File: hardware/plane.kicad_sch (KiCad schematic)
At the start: 44 parts, among them J1 USB_B_Micro, J2 Conn_Coaxial, J3 Conn_01x03, J4 Conn_01x03, J5 Conn_01x03, J6 Conn_01x03, Q1 BSS138, Q2 BSS138, U1 ESP32-WROOM-32, U2 AMS1117-3.3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

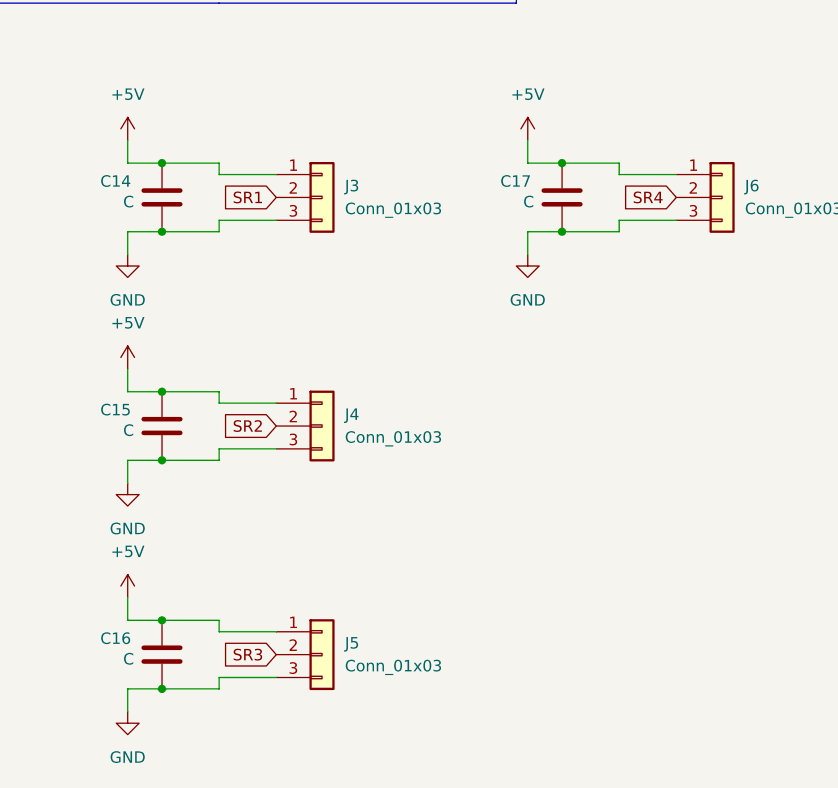
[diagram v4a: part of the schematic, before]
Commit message: add servo pin + wiring pcb
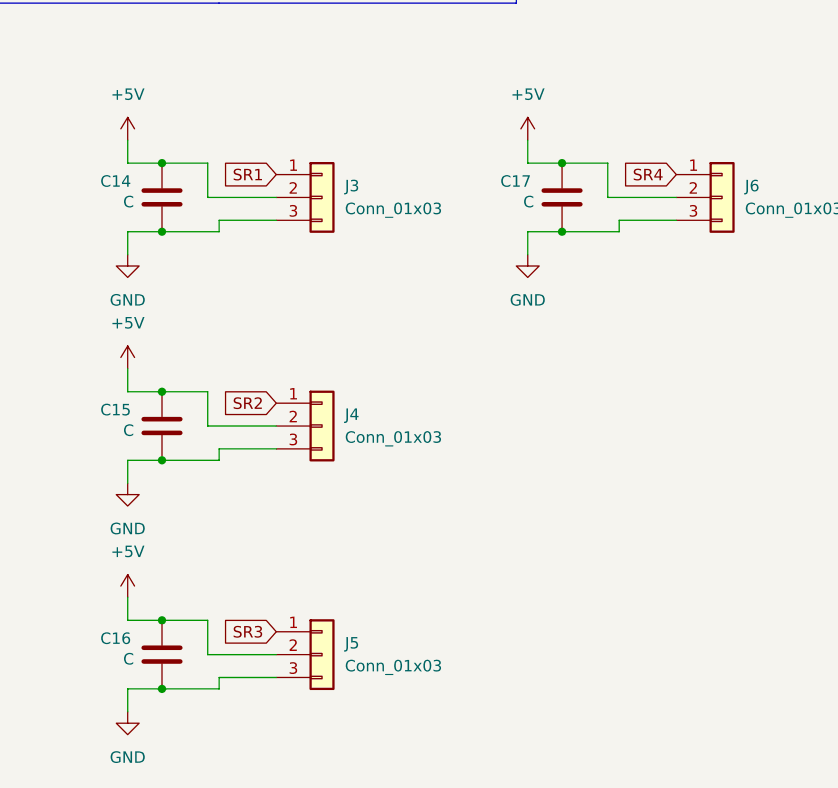
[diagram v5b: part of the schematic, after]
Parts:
- J3, J4, J5, J6: footprint (none) -> Connector_PinHeader_2.54mm:PinHeader_1x03_P2.54mm_Vertical
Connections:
- net +5V: now also J3.2 (Pin_2), J4.2 (Pin_2), J5.2 (Pin_2), J6.2 (Pin_2); no longer J3.1 (Pin_1), J4.1 (Pin_1), J5.1 (Pin_1), J6.1 (Pin_1)
- net SR1: now also J3.1 (Pin_1); no longer J3.2 (Pin_2)
- net SR2: now also J4.1 (Pin_1); no longer J4.2 (Pin_2)
- net SR3: now also J5.1 (Pin_1); no longer J5.2 (Pin_2)
- net SR4: now also J6.1 (Pin_1); no longer J6.2 (Pin_2)

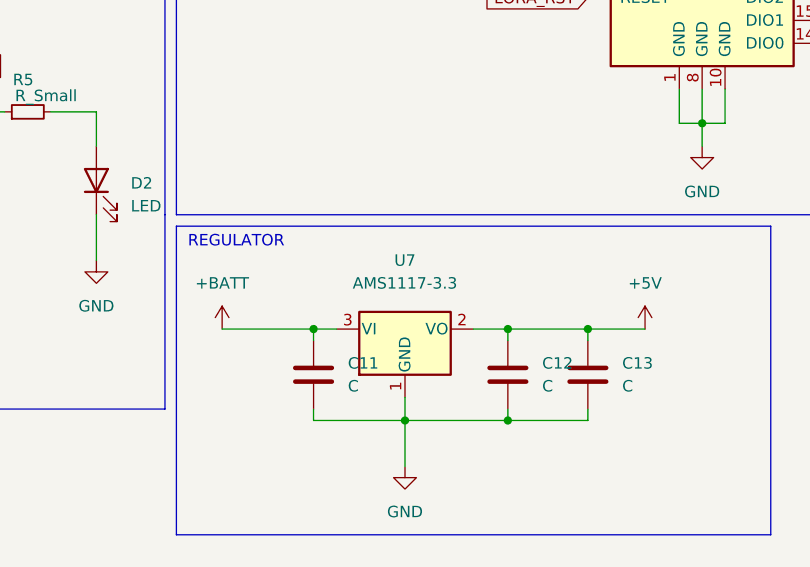
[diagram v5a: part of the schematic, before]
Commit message: wiring servo
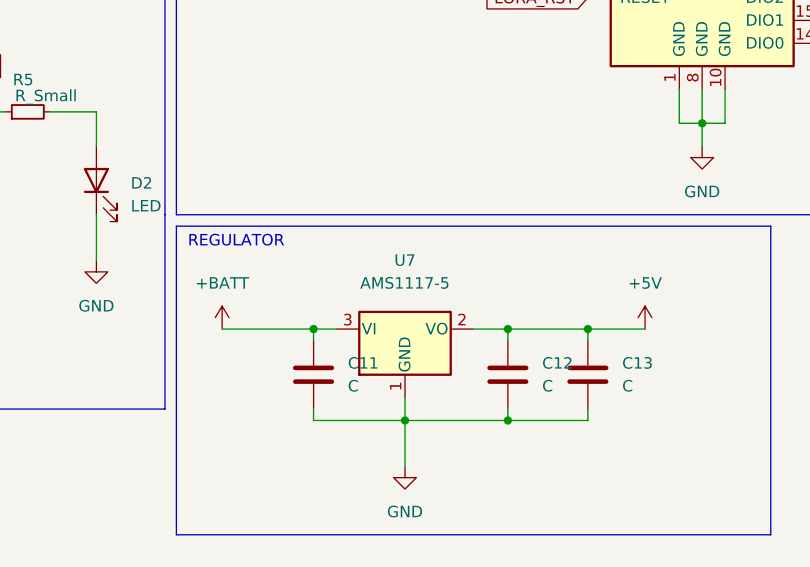
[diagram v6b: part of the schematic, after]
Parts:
- U7: value AMS1117-3.3 -> AMS1117-5
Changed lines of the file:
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@@
 			)
 		)
-		(property "Value" "AMS1117-3.3"
+		(property "Value" "AMS1117-5"
 			(at 137.16 129.54 0)
 			(effects

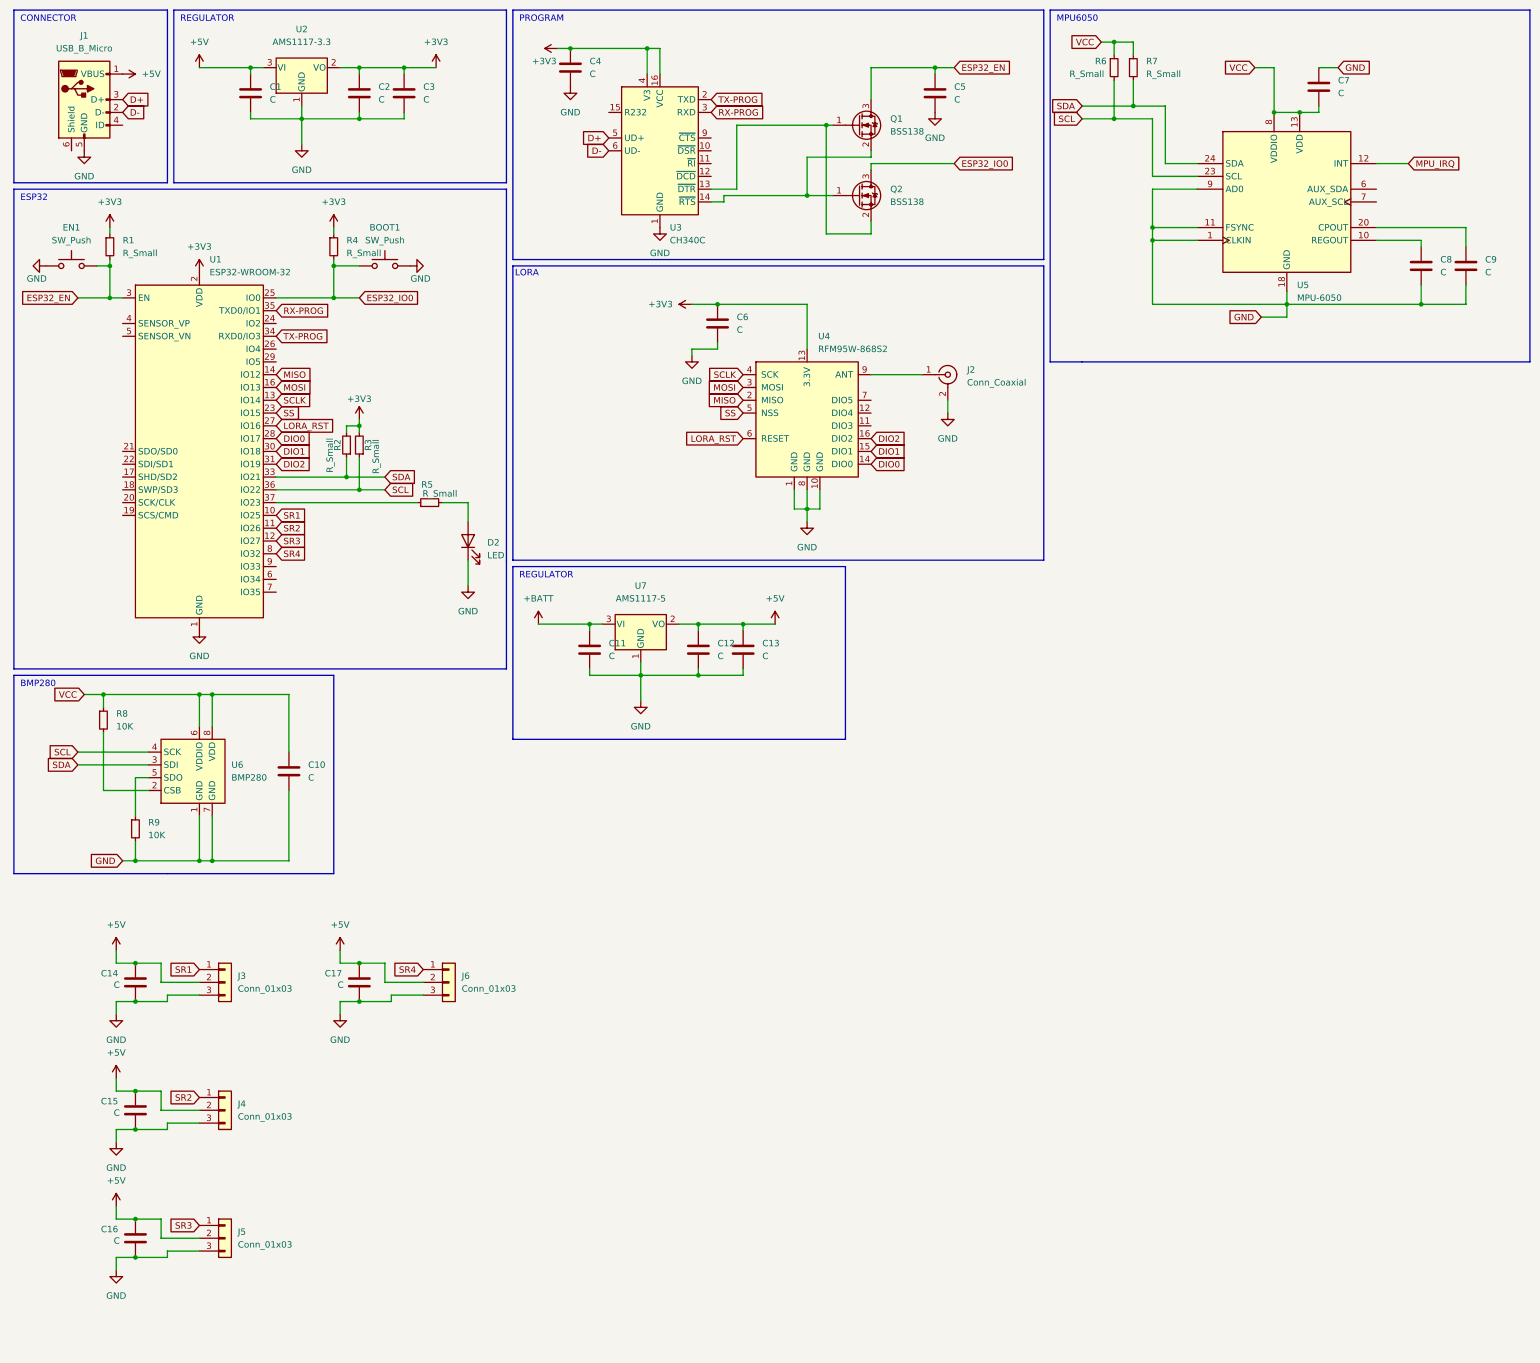
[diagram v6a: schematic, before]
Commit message: i2c wiring
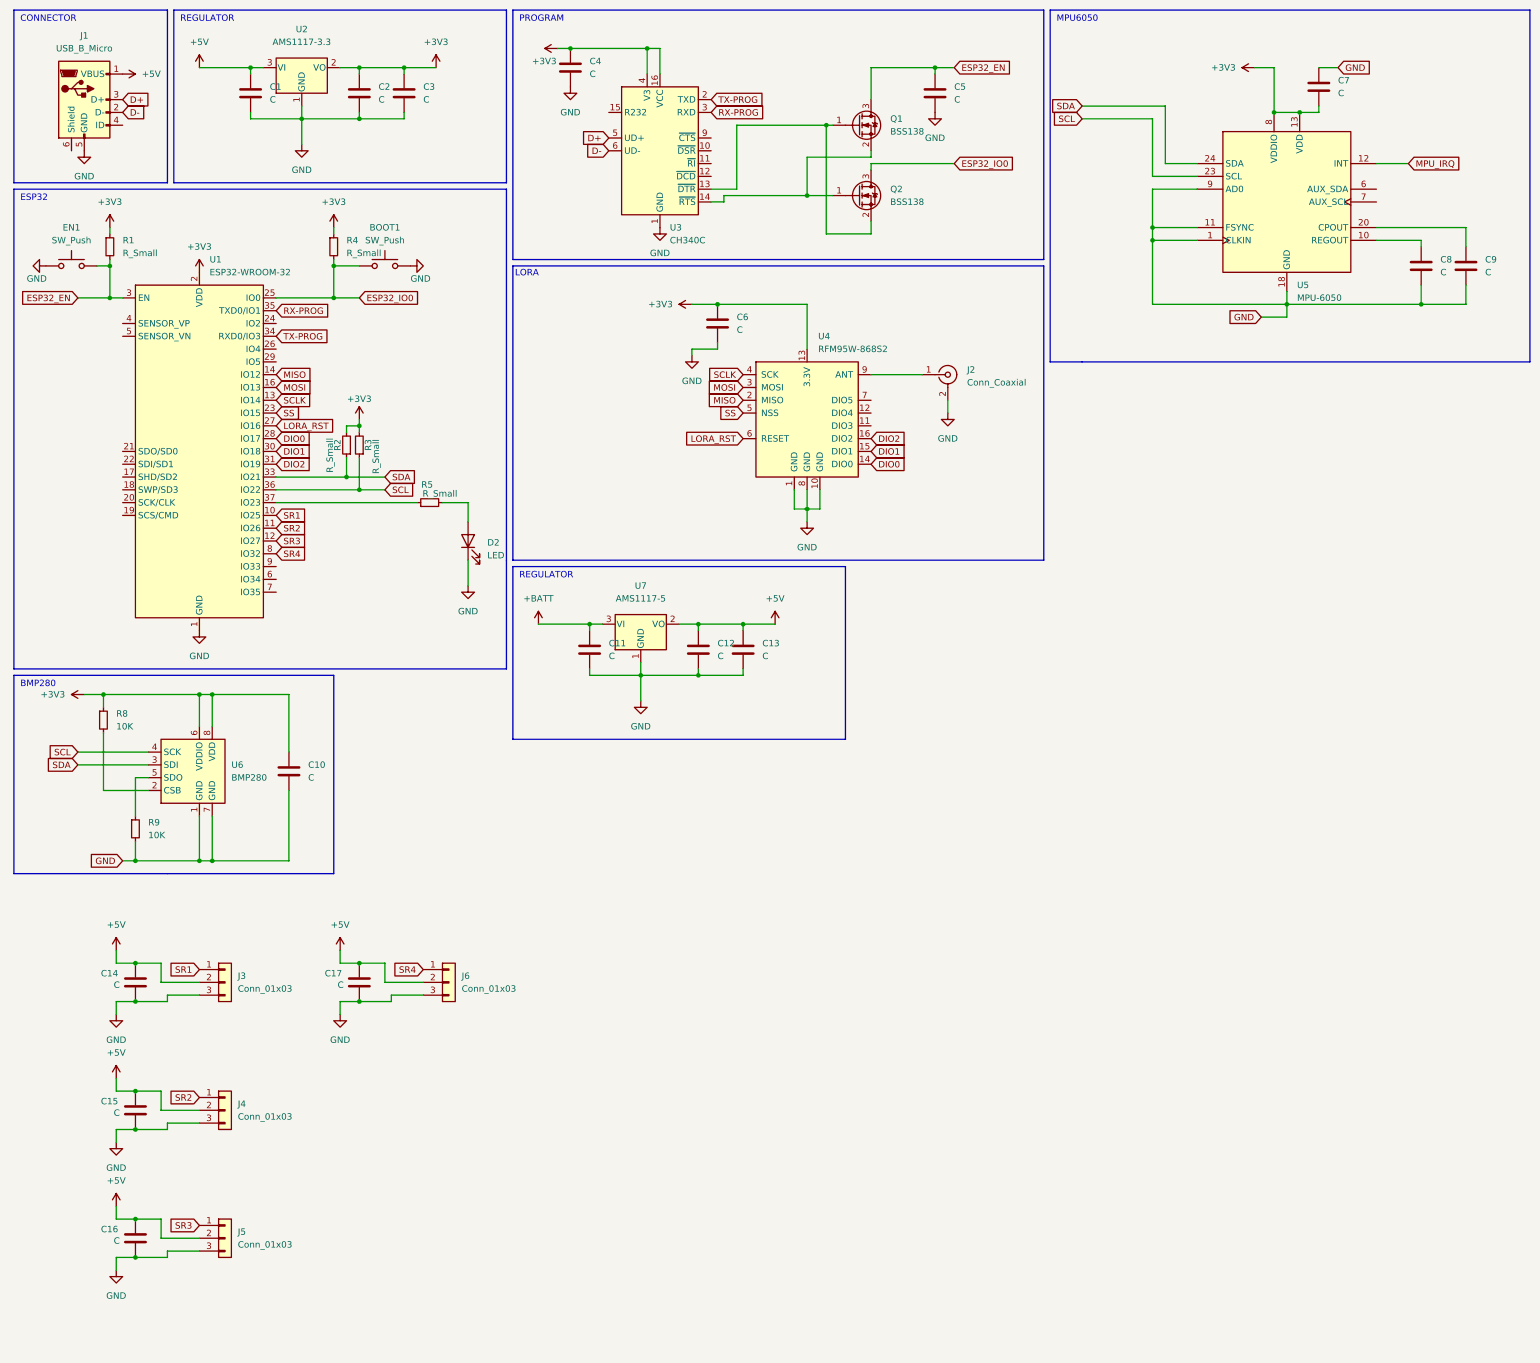
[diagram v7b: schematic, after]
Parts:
- removed R6, R7: R_Small, Resistor_SMD:R_0603_1608Metric, symbol Device:R_Small
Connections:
- net VCC is gone; now on net +3V3: C10.1, C7.2, R8.1, U5.13 (VDD), U5.8 (VDDIO), U6.6 (VDDIO), U6.8 (VDD)
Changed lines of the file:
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@@
 	)
 	(junction
-		(at 231.14 19.05)
-		(diameter 0)
-		(color 0 0 0 0)
-	)
-	(junction
 		(at 267.97 33.02)
 		(diameter 0)
@@
 	)
 	(junction
-		(at 234.95 31.75)
-		(diameter 0)
-		(color 0 0 0 0)
-	)
-	(junction
 		(at 157.48 134.62)
 		(diameter 0)
@@
 	)
 	(junction
-		(at 231.14 34.29)
-		(diameter 0)
-		(color 0 0 0 0)
-	)
-	(junction
 		(at 195.58 24.13)
 		(diameter 0)
@@
 	(wire
 		(pts
-			(xy 234.95 21.59) (xy 234.95 19.05)
-		)
-		(stroke
-			(width 0)
-			(type default)
-		)
-	)
-	(wire
-		(pts
 			(xy 49.53 148.59) (xy 52.07 148.59)
 		)
@@
 	(wire
 		(pts
-			(xy 231.14 21.59) (xy 231.14 19.05)
-		)
-		(stroke
-			(width 0)
-			(type default)
-		)
-	)
-	(wire
-		(pts
 			(xy 36.83 181.61) (xy 49.53 181.61)
 		)
@@
 	(wire
 		(pts
-			(xy 234.95 26.67) (xy 234.95 31.75)
-		)
-		(stroke
-			(width 0)
-			(type default)
-		)
-	)
-	(wire
-		(pts
 			(xy 87.63 208.28) (xy 87.63 209.55)
 		)
@@
 	(wire
 		(pts
-			(xy 231.14 26.67) (xy 231.14 34.29)
-		)
-		(stroke
-			(width 0)
-			(type default)
-		)
-	)
-	(wire
-		(pts
 			(xy 182.88 44.45) (xy 182.88 43.18)
 		)
@@
 	(wire
 		(pts
-			(xy 231.14 19.05) (xy 228.6 19.05)
-		)
-		(stroke
-			(width 0)
-			(type default)
-		)
-	)
-	(wire
-		(pts
 			(xy 152.4 80.01) (xy 147.32 80.01)
 		)
@@
 	(wire
 		(pts
-			(xy 231.14 34.29) (xy 238.76 34.29)
-		)
-		(stroke
-			(width 0)
-			(type default)
-		)
-	)
-	(wire
-		(pts
 			(xy 52.07 172.72) (xy 52.07 181.61)
 		)
@@
 	(wire
 		(pts
-			(xy 234.95 19.05) (xy 231.14 19.05)
-		)
-		(stroke
-			(width 0)
-			(type default)
-		)
-	)
-	(wire
-		(pts
 			(xy 76.2 69.85) (xy 76.2 63.5)
 		)
@@
 	(wire
 		(pts
-			(xy 224.79 31.75) (xy 234.95 31.75)
+			(xy 224.79 31.75) (xy 241.3 31.75)
 		)
 		(stroke
@@
 		)
 	)
-	(wire
-		(pts
-			(xy 234.95 31.75) (xy 241.3 31.75)
-		)
-		(stroke
-			(width 0)
-			(type default)
-		)
-	)
 	(polyline
 		(pts
@@
 	(wire
 		(pts
-			(xy 224.79 34.29) (xy 231.14 34.29)
+			(xy 224.79 34.29) (xy 238.76 34.29)
 		)
 		(stroke
@@
 		)
 	)
-	(global_label "VCC"
-		(shape input)
-		(at 26.67 148.59 180)
-		(fields_autoplaced yes)
-		(effects
-			(font
-				(size 1.27 1.27)
-			)
-			(justify right)
-		)
-		(property "Intersheetrefs" "${INTERSHEET_REFS}"
-			(at 20.6283 148.5106 0)
-			(effects
-				(font
-					(size 1.27 1.27)
-				)
-				(justify right)
-				(hide yes)
-			)
-		)
-	)
 	(global_label "GND"
 		(shape input)
@@
 		)
 	)
-	(global_label "VCC"
-		(shape input)
-		(at 228.6 19.05 180)
-		(fields_autoplaced yes)
-		(effects
-			(font
-				(size 1.27 1.27)
-			)
-			(justify right)
-		)
-		(property "Intersheetrefs" "${INTERSHEET_REFS}"
-			(at 222.5583 18.9706 0)
-			(effects
-				(font
-					(size 1.27 1.27)
-				)
-				(justify right)
-				(hide yes)
-			)
-		)
-	)
-	(global_label "VCC"
-		(shape input)
-		(at 259.08 24.13 180)
-		(fields_autoplaced yes)
-		(effects
-			(font
-				(size 1.27 1.27)
-			)
-			(justify right)
-		)
-		(property "Intersheetrefs" "${INTERSHEET_REFS}"
-			(at 253.0383 24.0506 0)
-			(effects
-				(font
-					(size 1.27 1.27)
-				)
-				(justify right)
-				(hide yes)
-			)
-		)
-	)
 	(global_label "LORA_RST"
 		(shape input)
@@
 	)
 	(symbol
-		(lib_id "Device:R_Small")
-		(at 231.14 24.13 0)
+		(lib_id "power:+3V3")
+		(at 26.67 148.59 90)
 		(unit 1)
 		(exclude_from_sim no)
@@
 		(on_board yes)
 		(dnp no)
-		(property "Reference" "R6"
-			(at 227.33 22.86 0)
+		(fields_autoplaced yes)
+		(property "Reference" "#PWR033"
+			(at 30.48 148.59 0)
 			(effects
 				(font
 					(size 1.27 1.27)
 				)
-				(justify left)
+				(hide yes)
 			)
 		)
-		(property "Value" "R_Small"
-			(at 222.25 25.4 0)
+		(property "Value" "+3V3"
+			(at 22.86 148.5899 90)
 			(effects
 				(font
@@
 			)
 		)
-		(property "Footprint" "Resistor_SMD:R_0603_1608Metric"
-			(at 231.14 24.13 0)
+		(property "Footprint" ""
+			(at 26.67 148.59 0)
 			(effects
 				(font
@@
 			)
 		)
-		(property "Datasheet" "~"
-			(at 231.14 24.13 0)
+		(property "Datasheet" ""
+			(at 26.67 148.59 0)
 			(effects
 				(font
@@
 		)
 		(property "Description" ""
-			(at 231.14 24.13 0)
+			(at 26.67 148.59 0)
 			(effects
 				(font
@@
 		(pin "1"
 		)
-		(pin "2"
-		)
 		(instances
 			(project "plane"
 				(path "/da86c4d3-eb89-47ad-a94a-ba8dff9acc70"
-					(reference "R6")
+					(reference "#PWR033")
 					(unit 1)
 				)
@@
 	)
 	(symbol
+		(lib_id "power:+3V3")
+		(at 259.08 24.13 90)
+		(unit 1)
+		(exclude_from_sim no)
+		(in_bom yes)
+		(on_board yes)
+		(dnp no)
+		(fields_autoplaced yes)
+		(property "Reference" "#PWR034"
+			(at 262.89 24.13 0)
+			(effects
+				(font
+					(size 1.27 1.27)
+				)
+				(hide yes)
+			)
+		)
+		(property "Value" "+3V3"
+			(at 255.27 24.1299 90)
+			(effects
+				(font
+					(size 1.27 1.27)
+				)
+				(justify left)
+			)
+		)
+		(property "Footprint" ""
+			(at 259.08 24.13 0)
+			(effects
+				(font
+					(size 1.27 1.27)
+				)
+				(hide yes)
+			)
+		)
+		(property "Datasheet" ""
+			(at 259.08 24.13 0)
+			(effects
+				(font
+					(size 1.27 1.27)
+				)
+				(hide yes)
+			)
+		)
+		(property "Description" ""
+			(at 259.08 24.13 0)
+			(effects
+				(font
+					(size 1.27 1.27)
+				)
+				(hide yes)
+			)
+		)
+		(pin "1"
+		)
+		(instances
+			(project "plane"
+				(path "/da86c4d3-eb89-47ad-a94a-ba8dff9acc70"
+					(reference "#PWR034")
+					(unit 1)
+				)
+			)
+		)
+	)
+	(symbol
 		(lib_id "Transistor_FET:BSS138")
 		(at 180.34 35.56 0)
@@
 					(unit 1)
 				)
-			)
-		)
-	)
-	(symbol
-		(lib_id "Device:R_Small")
-		(at 234.95 24.13 0)
-		(unit 1)
-		(exclude_from_sim no)
-		(in_bom yes)
-		(on_board yes)
-		(dnp no)
-		(fields_autoplaced yes)
-		(property "Reference" "R7"
-			(at 237.49 22.8599 0)
-			(effects
-				(font
-					(size 1.27 1.27)
-				)
-				(justify left)
-			)
-		)
-		(property "Value" "R_Small"
-			(at 237.49 25.3999 0)
-			(effects
-				(font
-					(size 1.27 1.27)
-				)
-				(justify left)
-			)
-		)
-		(property "Footprint" "Resistor_SMD:R_0603_1608Metric"
-			(at 234.95 24.13 0)
-			(effects
-				(font
-					(size 1.27 1.27)
-				)
-				(hide yes)
-			)
-		)
-		(property "Datasheet" "~"
-			(at 234.95 24.13 0)
-			(effects
-				(font
-					(size 1.27 1.27)
-				)
-				(hide yes)
-			)
-		)
-		(property "Description" ""
-			(at 234.95 24.13 0)
-			(effects
-				(font
-					(size 1.27 1.27)
-				)
-				(hide yes)
-			)
-		)
-		(pin "1"
-		)
-		(pin "2"
-		)
-		(instances
-			(project "plane"
-				(path "/da86c4d3-eb89-47ad-a94a-ba8dff9acc70"
-					(reference "R7")
-					(unit 1)
-				)
